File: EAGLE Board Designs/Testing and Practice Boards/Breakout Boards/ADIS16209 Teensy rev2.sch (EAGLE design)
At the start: 9 parts

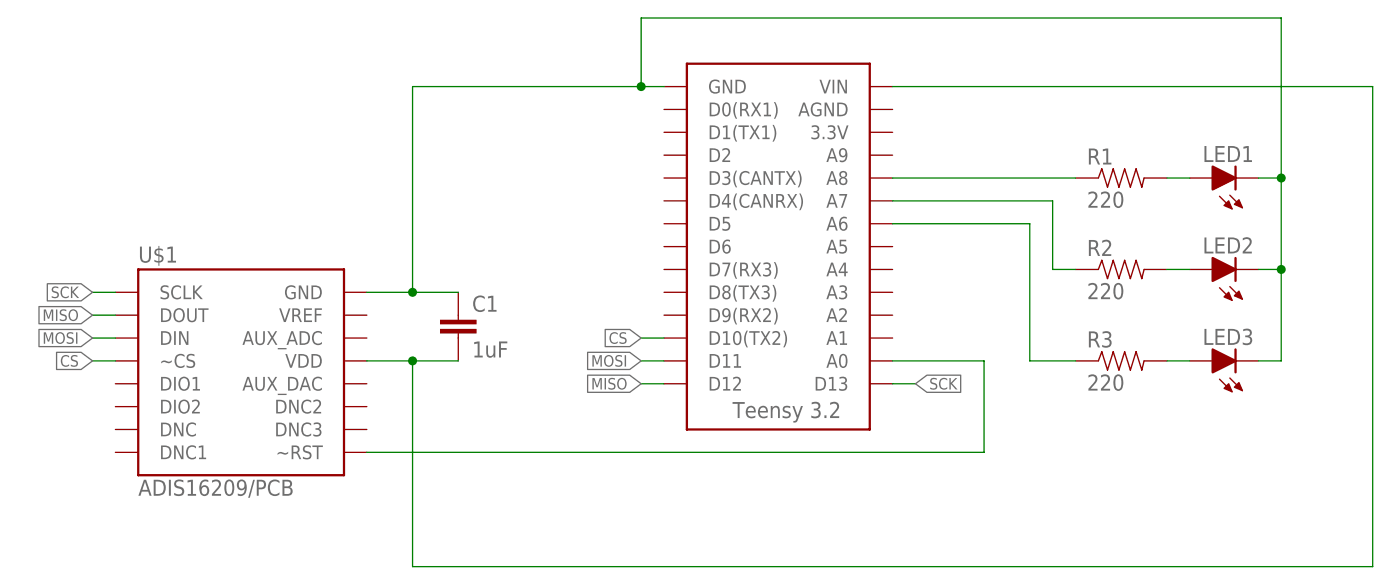
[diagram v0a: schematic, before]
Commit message: updated the rev2 to switch to 3.3V supply and changed the layout so the dude at electronics lab will not be mad at Yvonne
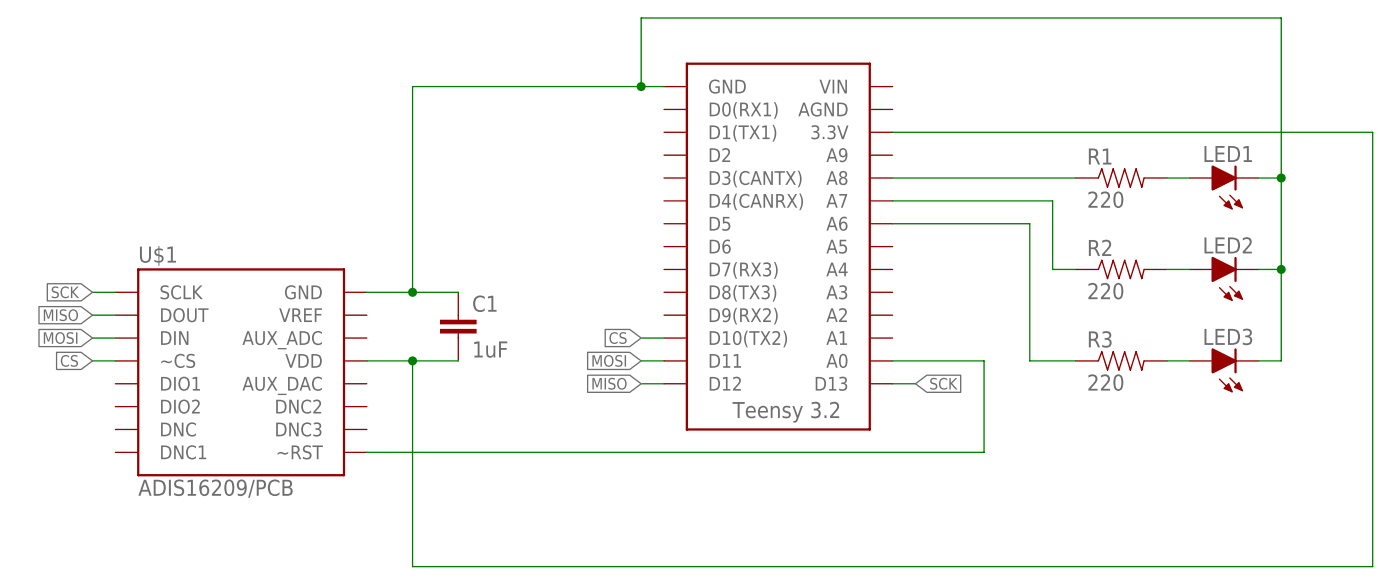
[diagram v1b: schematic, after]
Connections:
- net +3V3: now also U$2.3.3V; no longer U$2.VIN
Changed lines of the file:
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@@
 <wire x1="25.4" y1="30.48" x2="25.4" y2="7.62" width="0.1524" layer="91"/>
 <wire x1="25.4" y1="7.62" x2="132.08" y2="7.62" width="0.1524" layer="91"/>
-<wire x1="132.08" y1="7.62" x2="132.08" y2="60.96" width="0.1524" layer="91"/>
-<pinref part="U$2" gate="G$1" pin="VIN"/>
-<wire x1="132.08" y1="60.96" x2="78.74" y2="60.96" width="0.1524" layer="91"/>
+<wire x1="132.08" y1="7.62" x2="132.08" y2="55.88" width="0.1524" layer="91"/>
 <pinref part="C1" gate="G$1" pin="2"/>
 <wire x1="30.48" y1="30.48" x2="25.4" y2="30.48" width="0.1524" layer="91"/>
 <junction x="25.4" y="30.48"/>
+<pinref part="U$2" gate="G$1" pin="3.3V"/>
+<wire x1="78.74" y1="55.88" x2="132.08" y2="55.88" width="0.1524" layer="91"/>
 </segment>
 </net>
